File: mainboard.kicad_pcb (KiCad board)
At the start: 2 copper layers, 180 x 87 mm, 16 parts, among them J1 Raspi Pi Zero 2W, J2 LCD, J3 Keyboard, J4 USB_C_Receptacle_USB2.0, J5 Conn_02x20_Odd_Even, J6 Conn_02x20_Odd_Even, U1 MCP23017_SO

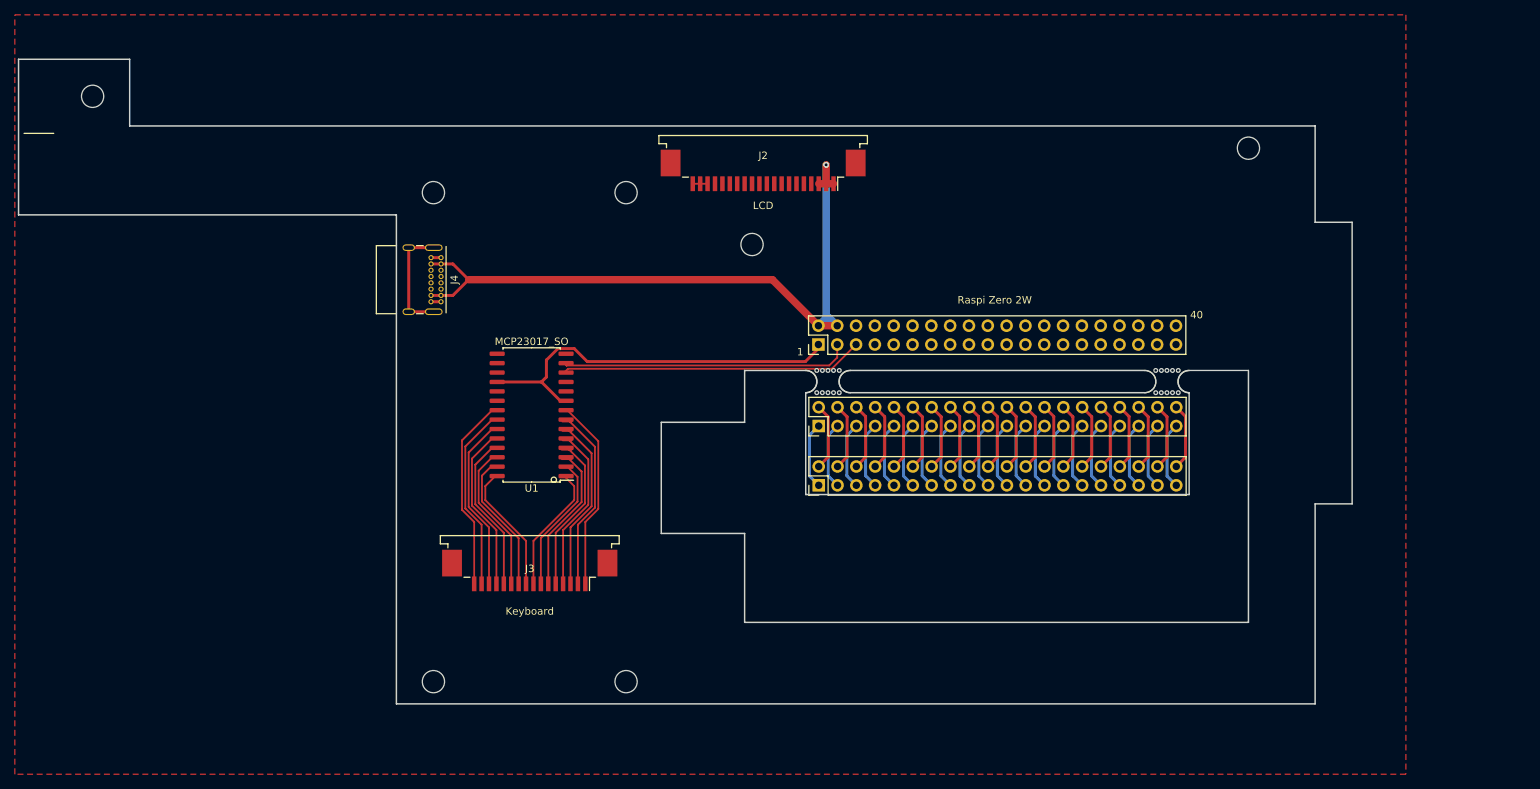
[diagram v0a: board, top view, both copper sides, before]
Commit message: adding logic converter and power supply
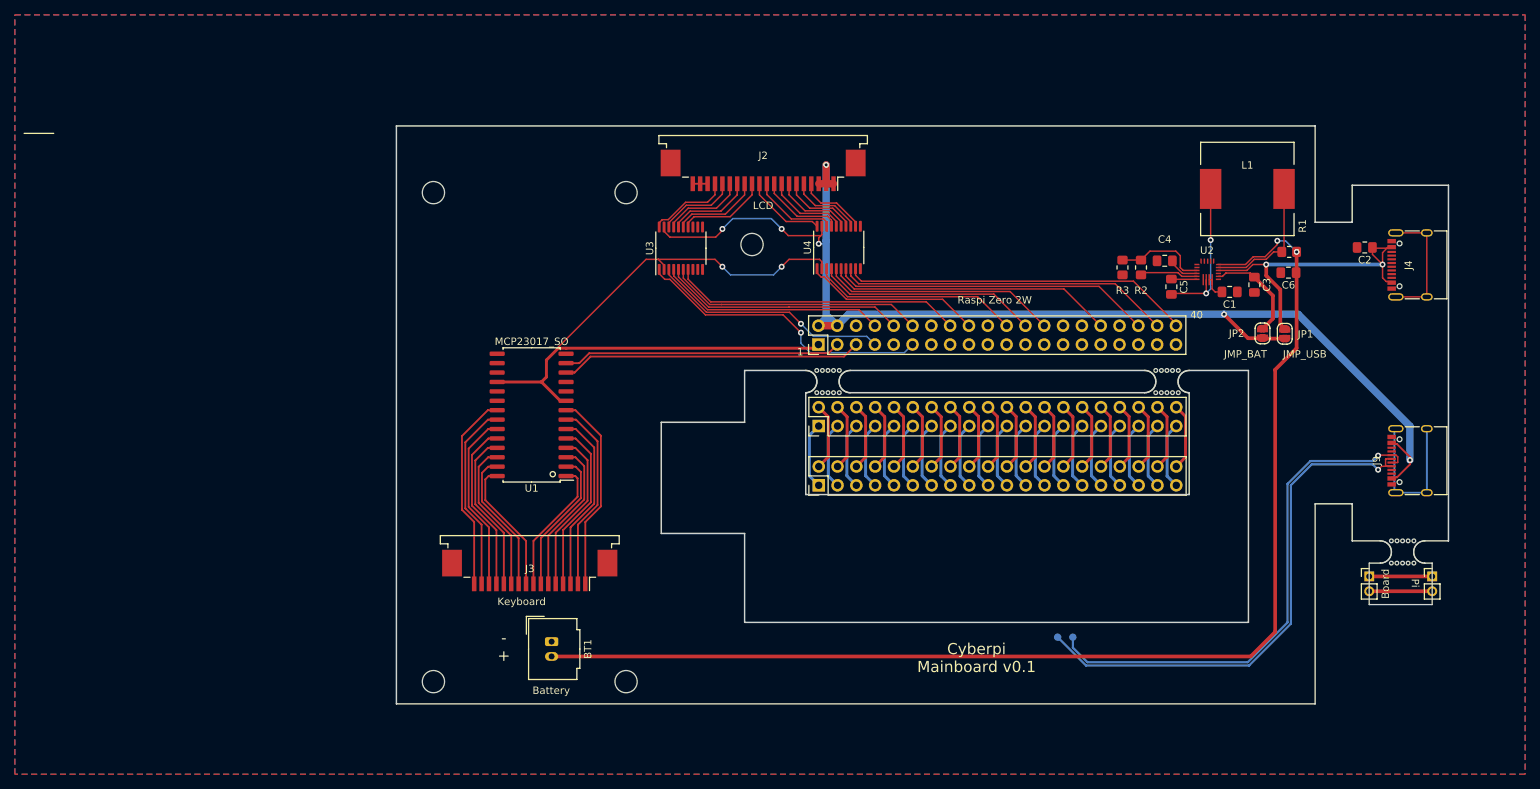
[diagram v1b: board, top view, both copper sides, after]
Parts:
- removed the REF** at (192.9, 59.4)
- removed the REF** at (36.9, 52.4)
- added BT1: Battery, Connector_Molex:Molex_MicroClasp_55932-0230_1x02_P2.00mm_Vertical, F.Cu at (98.8, 126.0)
- added C1: 10u 16V, Capacitor_SMD:C_0805_2012Metric_Pad1.18x1.45mm_HandSolder, F.Cu at (190.3, 78.8)
- added C2: 1u 16V, Capacitor_SMD:C_0805_2012Metric_Pad1.18x1.45mm_HandSolder, F.Cu at (208.6, 72.8)
- added C3: 10u 16V, Capacitor_SMD:C_0805_2012Metric_Pad1.18x1.45mm_HandSolder, F.Cu at (193.7, 77.8)
- added C4: 2.2u 6.3V, Capacitor_SMD:C_0805_2012Metric_Pad1.18x1.45mm_HandSolder, F.Cu at (181.6, 74.6)
- added C5: 470n 10V, Capacitor_SMD:C_0805_2012Metric_Pad1.18x1.45mm_HandSolder, F.Cu at (182.5, 78.1)
- added C6: 22u 10V, Capacitor_SMD:C_0805_2012Metric_Pad1.18x1.45mm_HandSolder, F.Cu at (198.3, 76.2)
- added J10: USBDataBoard, Connector_PinHeader_2.00mm:PinHeader_1x02_P2.00mm_Vertical, F.Cu at (209.2, 117.2)
- added J11: DM, TestPoint:TestPoint_Pad_D1.0mm, B.Cu at (167.1, 125.4)
- added J7: DP, TestPoint:TestPoint_Pad_D1.0mm, B.Cu at (169.2, 125.4)
- added J8: USBDataPi, Connector_PinHeader_2.00mm:PinHeader_1x02_P2.00mm_Vertical, F.Cu at (217.7, 117.2)
- added J9: USB Data, Connector_USB:USB_C_Receptacle_XKB_U262-16XN-4BVC11, F.Cu at (215.9, 101.6)
- added JP1: JMP_USB, Jumper:SolderJumper-2_P1.3mm_Open_RoundedPad1.0x1.5mm, F.Cu at (197.8, 84.5)
- added JP2: JMP_BAT, Jumper:SolderJumper-2_P1.3mm_Open_RoundedPad1.0x1.5mm, F.Cu at (194.8, 84.4)
- added L1: 1uH, Inductor_SMD:L_12x12mm_H4.5mm, F.Cu at (192.7, 64.9)
- added R1: 10m, Resistor_SMD:R_0805_2012Metric_Pad1.20x1.40mm_HandSolder, F.Cu at (198.4, 73.4)
- added R2: 10k, Resistor_SMD:R_0805_2012Metric_Pad1.20x1.40mm_HandSolder, F.Cu at (178.4, 75.5)
- added R3: 10k, Resistor_SMD:R_0805_2012Metric_Pad1.20x1.40mm_HandSolder, F.Cu at (175.9, 75.5)
- added U2: MP2696A, Library:QFN-21, F.Cu at (187.4, 76.1)
- added U3: TXS0108EPW, Package_SO:TSSOP-20_4.4x6.5mm_P0.65mm, F.Cu at (116.3, 72.9)
- added U4: TXS0108EPW, Package_SO:TSSOP-20_4.4x6.5mm_P0.65mm, F.Cu at (137.6, 72.8)
- added mouse-bite-3mm-slot: VAL**, Library:mouse-bite-3mm-slot, F.Cu at (213.7, 113.9)
- J4: value USB_C_Receptacle_USB2.0 -> USB Power; footprint Connector_USB:USB_C_Receptacle_GCT_USB4085 -> Connector_USB:USB_C_Receptacle_XKB_U262-16XN-4BVC11
- moved J4 132.0 mm to (215.9, 75.2), turned to 90 degrees
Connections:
- J1 pad 13: /GPIO_27 -> unconnected-(J1-Pad13)
- J1 pad 14: GND -> unconnected-(J1-Pad14)
- J1 pad 15: /GPIO_22 -> unconnected-(J1-Pad15)
- J1 pad 17: +3V3 -> unconnected-(J1-Pad17)
- J1 pad 19: /GPIO_10 -> unconnected-(J1-Pad19)
- J1 pad 20: GND -> unconnected-(J1-Pad20)
- J1 pad 21: /GPIO_9 -> unconnected-(J1-Pad21)
- J1 pad 23: /GPIO_11 -> unconnected-(J1-Pad23)
- J1 pad 27: /EEPROM_DATA -> unconnected-(J1-Pad27)
- J1 pad 28: /SCL0 -> unconnected-(J1-Pad28)
- J1 pad 29: /GPIO_5 -> unconnected-(J1-Pad29)
- J1 pad 30: GND -> unconnected-(J1-Pad30)
- J1 pad 31: /GPIO_6 -> unconnected-(J1-Pad31)
- J1 pad 33: /GPIO_13 -> unconnected-(J1-Pad33)
- J1 pad 34: GND -> unconnected-(J1-Pad34)
- J1 pad 35: /GPIO_19 -> unconnected-(J1-Pad35)
- J1 pad 37: /GPIO_26 -> unconnected-(J1-Pad37)
- J1 pad 6: GND -> unconnected-(J1-Pad6)
- J1 pad 9: GND -> unconnected-(J1-Pad9)
- J4 pad A4: +5V -> /Power Circuit/USBPWR
- J4 pad A9: +5V -> /Power Circuit/USBPWR
- J4 pad B4: +5V -> /Power Circuit/USBPWR
- J4 pad B9: +5V -> /Power Circuit/USBPWR
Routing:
- net Net-(BT1-Pad2): track 0.00 -> 164.4 mm, vias 0 -> 2
- net +5V: track 92.8 -> 164.8 mm, vias 1 -> 6
- net /D-: track 0.00 -> 71.9 mm, vias 0 -> 1
- net /D+: track 0.00 -> 70.3 mm, vias 0 -> 1
- net /GPIO_21: track 0.00 -> 47.1 mm
- net /GPIO_20: track 0.00 -> 45.1 mm
- net /Power Circuit/USBPWR: track 0.00 -> 44.2 mm, vias 0 -> 2
- net +3V3: track 52.9 -> 96.3 mm, vias 0 -> 2
- net /GPIO_16: track 0.00 -> 43.2 mm
- net /GPIO_17: track 0.00 -> 40.5 mm, vias 0 -> 1
- net /GPIO_23: track 0.00 -> 39.3 mm
- net /GPIO_12: track 0.00 -> 38.8 mm
- net /GPIO_18: track 0.00 -> 34.8 mm
- net /GPIO_15: track 0.00 -> 32.8 mm
- net /GPIO_4: track 0.00 -> 32.4 mm, vias 0 -> 1
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- added copper zone on B.Cu, net GND
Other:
- board size 180 x 87 mm -> 142 x 78 mm
- rule pad_to_mask_clearance: 0.051 -> 0
- board text added: "- +"
- board text added: "3mm"
- board text added: "Board"
- board text added: "Cyberpi Mainboard v0.1"
- board text added: "Data"
- board text added: "Pi"
- board text added: "Power"

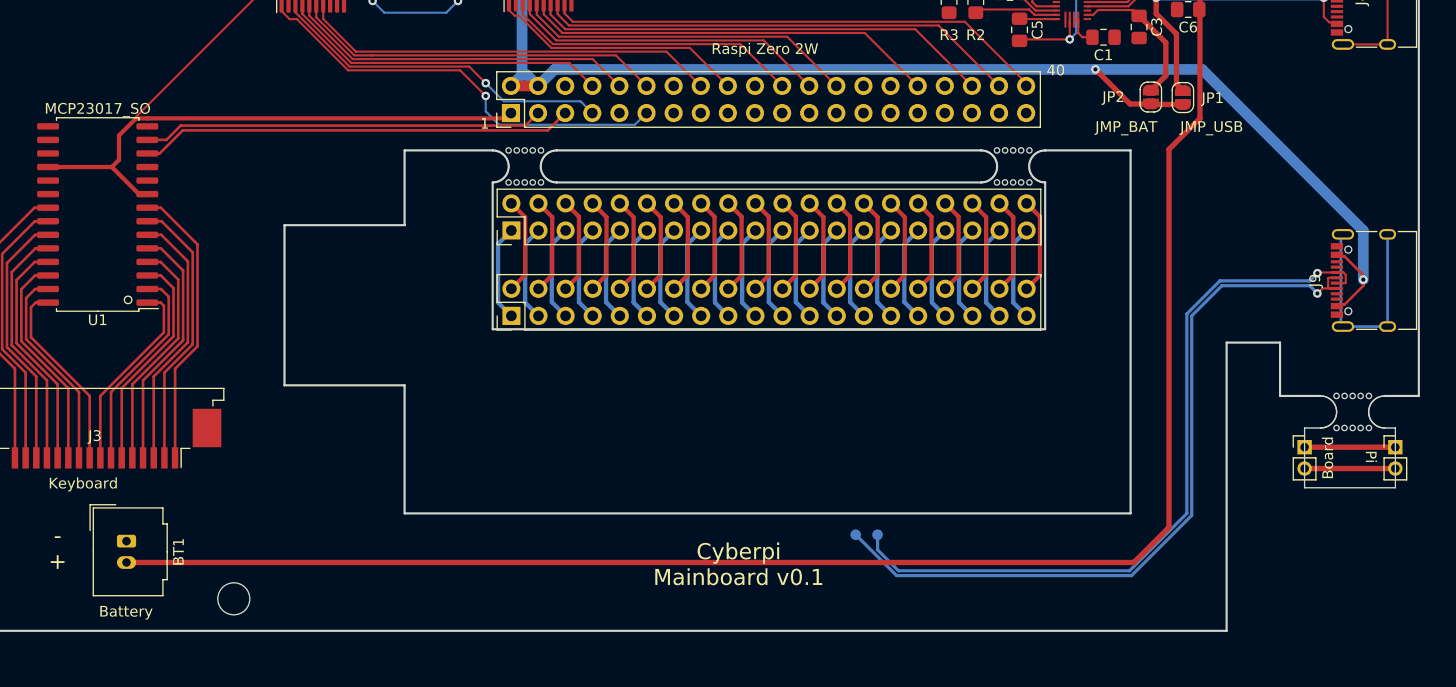
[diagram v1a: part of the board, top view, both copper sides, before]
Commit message: Adding switch to power
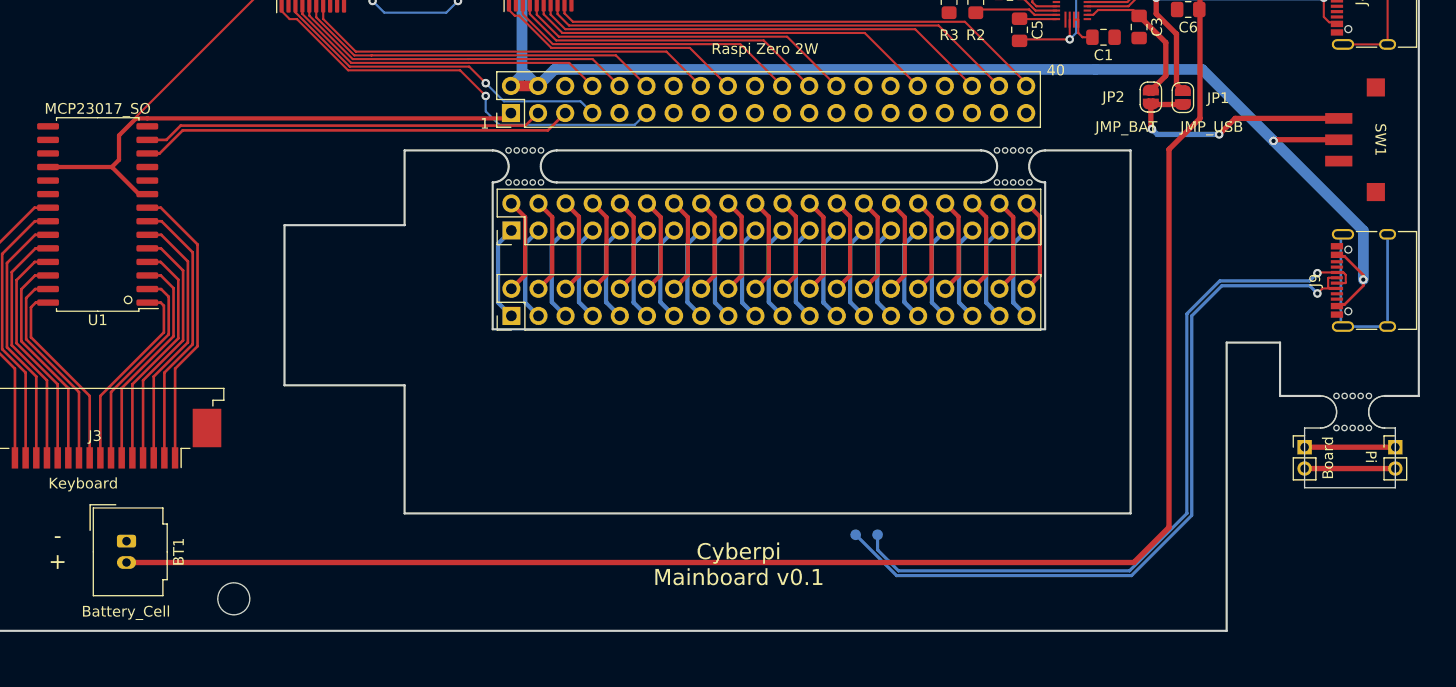
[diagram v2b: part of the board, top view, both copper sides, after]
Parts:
- added SW1: SW_SPST, Library:SS312SAH4-R, F.Cu at (215.5, 88.4)
- BT1: value Battery -> Battery_Cell
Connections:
- JP1 pad 2: +5V -> Net-(JP1-Pad2)
- JP2 pad 2: +5V -> Net-(JP1-Pad2)
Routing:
- net Net-(JP1-Pad2): track 0.00 -> 23.7 mm, vias 0 -> 2
- net +5V: track 164.8 -> 161.4 mm
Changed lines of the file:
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@@
   (net 151 "unconnected-(J1-Pad35)")
   (net 152 "unconnected-(J1-Pad37)")
+  (net 153 "Net-(JP1-Pad2)")
   (footprint "MountingHole:MountingHole_3mm" locked (layer "F.Cu")
     (at 108.86 131.4)
@@
       (effects (font (size 1 1) (thickness 0.15)))
     )
-    (fp_text value "Battery" (at 6.6 0.05 180) (layer "F.SilkS")
+    (fp_text value "Battery_Cell" (at 6.6 0.05 180) (layer "F.SilkS")
       (effects (font (size 1 1) (thickness 0.15)))
     )
@@
       ))
     (pad "2" smd custom (at 0.65 0 270) (size 1 0.5) (layers "F.Cu" "F.Mask")
-      (net 1 "+5V") (pinfunction "B") (pintype "passive") (zone_connect 2)
+      (net 153 "Net-(JP1-Pad2)") (pinfunction "B") (pintype "passive") (zone_connect 2)
       (options (clearance outline) (anchor rect))
       (primitives
@@
     (property "Sheetname" "")
     (attr exclude_from_pos_files)
-    (fp_text reference "JP1" (at 0.05 -2.8 180) (layer "F.SilkS")
+    (fp_text reference "JP1" (at 0.05 -3.3 180) (layer "F.SilkS")
       (effects (font (size 1 1) (thickness 0.15)))
     )
@@
       ))
     (pad "2" smd custom (at 0.65 0 270) (size 1 0.5) (layers "F.Cu" "F.Mask")
-      (net 1 "+5V") (pinfunction "B") (pintype "passive") (zone_connect 2)
+      (net 153 "Net-(JP1-Pad2)") (pinfunction "B") (pintype "passive") (zone_connect 2)
       (options (clearance outline) (anchor rect))
       (primitives
@@
     )
   )
+  (footprint "Library:SS312SAH4-R" (layer "F.Cu")
+    (at 215.46 88.4 180)
+    (property "Sheetfile" "mainboard.kicad_sch")
+    (property "Sheetname" "")
+    (attr smd)
+    (fp_text reference "SW1" (at -0.8 0 270 unlocked) (layer "F.SilkS")
+      (effects (font (size 1 1) (thickness 0.15)))
+    )
+    (fp_text value "SW_SPST" (at 0.9 -0.1 270 unlocked) (layer "F.Fab")
+      (effects (font (size 1 1) (thickness 0.15)))
+    )
+    (fp_text user "${REFERENCE}" (at -0.8 0 270 unlocked) (layer "F.Fab")
+      (effects (font (size 1 1) (thickness 0.15)))
+    )
+    (fp_rect (start -1.8 2) (end -3.8 -2) (layer "F.Fab") (width 0.05) (fill none))
+    (fp_rect (start -1.8 -4.6) (end 2.2 4.6) (layer "F.Fab") (width 0.05) (fill none))
+    (pad "1" smd rect (at 3.1 2 180) (size 2.55 1) (layers "F.Cu" "F.Paste" "F.Mask")
+      (net 153 "Net-(JP1-Pad2)") (pinfunction "A") (pintype "passive"))
+    (pad "2" smd rect (at 3.1 0 180) (size 2.55 1) (layers "F.Cu" "F.Paste" "F.Mask")
+      (net 1 "+5V") (pinfunction "B") (pintype "passive"))
+    (pad "3" smd rect (at 3.1 -2 180) (size 2.55 1) (layers "F.Cu" "F.Paste" "F.Mask"))
+    (pad "NC" smd rect (at -0.375 4.9 180) (size 1.7 1.7) (layers "F.Cu" "F.Paste" "F.Mask"))
+    (pad "NC" smd rect (at -0.375 -4.9 180) (size 1.7 1.7) (layers "F.Cu" "F.Paste" "F.Mask"))
+  )
   (footprint "Capacitor_SMD:C_0805_2012Metric_Pad1.18x1.45mm_HandSolder" (layer "F.Cu")
     (at 198.26 76.2 180)
@@
   (segment (start 212.19 99.33) (end 212.905727 99.33) (width 0.25) (layer "F.Cu") (net 1))
   (segment (start 214.66 102.075727) (end 214.66 101.5) (width 0.25) (layer "F.Cu") (net 1))
-  (segment (start 192.81 85.05) (end 189.570489 81.810489) (width 0.5) (layer "F.Cu") (net 1))
   (segment (start 120.957038 71.4) (end 114.765705 71.4) (width 0.2) (layer "F.Cu") (net 1))
-  (segment (start 197.76 85.1) (end 194.81 85.1) (width 0.5) (layer "F.Cu") (net 1))
   (segment (start 114.765705 71.4) (end 113.985 70.619295) (width 0.2) (layer "F.Cu") (net 1))
-  (segment (start 194.81 85.1) (end 194.76 85.05) (width 0.5) (layer "F.Cu") (net 1))
   (segment (start 113.985 70.619295) (end 113.985 70.0375) (width 0.2) (layer "F.Cu") (net 1))
   (segment (start 214.66 101.084273) (end 214.66 101.5) (width 0.25) (layer "F.Cu") (net 1))
@@
   (segment (start 135.86 64.2) (end 134.864511 64.2) (width 1) (layer "F.Cu") (net 1))
   (segment (start 135.285 71.075) (end 135.16 71.2) (width 0.2) (layer "F.Cu") (net 1))
+  (segment (start 206.36 88.4) (end 206.250688 88.509312) (width 0.5) (layer "F.Cu") (net 1))
   (segment (start 137.36 83.36) (end 134.82 83.36) (width 1) (layer "F.Cu") (net 1))
   (segment (start 212.905727 99.33) (end 214.66 101.084273) (width 0.25) (layer "F.Cu") (net 1))
   (segment (start 129.86 70.3) (end 130.76 71.2) (width 0.2) (layer "F.Cu") (net 1))
-  (segment (start 194.76 85.05) (end 192.81 85.05) (width 0.5) (layer "F.Cu") (net 1))
   (segment (start 212.19 103.83) (end 212.905727 103.83) (width 0.25) (layer "F.Cu") (net 1))
   (segment (start 134.86 71.5) (end 134.86 72.3) (width 0.2) (layer "F.Cu") (net 1))
   (segment (start 135.285 69.9375) (end 135.285 71.075) (width 0.2) (layer "F.Cu") (net 1))
+  (segment (start 212.36 88.4) (end 206.36 88.4) (width 0.5) (layer "F.Cu") (net 1))
   (segment (start 135.86 64.2) (end 135.86 61.65) (width 1) (layer "F.Cu") (net 1))
   (segment (start 212.905727 103.83) (end 214.66 102.075727) (width 0.25) (layer "F.Cu") (net 1))
@@
   (segment (start 121.86 70.497038) (end 120.957038 71.4) (width 0.2) (layer "F.Cu") (net 1))
   (segment (start 135.86 64.2) (end 136.86 64.2) (width 1) (layer "F.Cu") (net 1))
-  (via (at 189.570489 81.810489) (size 0.8) (drill 0.4) (layers "F.Cu" "B.Cu") (net 1))
   (via (at 135.86 61.65) (size 0.8) (drill 0.4) (layers "F.Cu" "B.Cu") (net 1))
   (via (at 134.86 72.3) (size 0.8) (drill 0.4) (layers "F.Cu" "B.Cu") (net 1))
   (via (at 214.66 101.5) (size 0.8) (drill 0.4) (layers "F.Cu" "B.Cu") (net 1))
   (via (at 129.86 70.3) (size 0.8) (drill 0.4) (layers "F.Cu" "B.Cu") (net 1))
+  (via (at 206.250688 88.509312) (size 0.8) (drill 0.4) (layers "F.Cu" "B.Cu") (net 1))
   (via (at 121.86 70.3) (size 0.8) (drill 0.4) (layers "F.Cu" "B.Cu") (net 1))
   (segment (start 135.86 82.32) (end 134.82 83.36) (width 1) (layer "B.Cu") (net 1))
@@
   (segment (start 134.86 72.3) (end 135.46 72.3) (width 0.2) (layer "B.Cu") (net 1))
   (segment (start 121.86 70.3) (end 123.26 68.9) (width 0.2) (layer "B.Cu") (net 1))
+  (segment (start 206.250688 88.509312) (end 214.66 96.918623) (width 1) (layer "B.Cu") (net 1))
   (segment (start 128.46 68.9) (end 129.86 70.3) (width 0.2) (layer "B.Cu") (net 1))
   (segment (start 123.26 68.9) (end 128.46 68.9) (width 0.2) (layer "B.Cu") (net 1))
@@
   (segment (start 138.909511 81.810489) (end 189.570489 81.810489) (width 1) (layer "B.Cu") (net 1))
   (segment (start 137.36 83.36) (end 138.909511 81.810489) (width 1) (layer "B.Cu") (net 1))
+  (segment (start 199.551866 81.810489) (end 206.250688 88.509312) (width 1) (layer "B.Cu") (net 1))
   (segment (start 189.570489 81.810489) (end 199.551866 81.810489) (width 1) (layer "B.Cu") (net 1))
-  (segment (start 199.551866 81.810489) (end 214.66 96.918623) (width 1) (layer "B.Cu") (net 1))
   (segment (start 135.86 61.65) (end 135.86 71.9) (width 1) (layer "B.Cu") (net 1))
   (segment (start 136.585 76.625) (end 136.585 75.6625) (width 0.2) (layer "F.Cu") (net 2))
@@
   (segment (start 193.66 76.8) (end 196.16 79.3) (width 0.5) (layer "F.Cu") (net 129))
   (segment (start 189.359022 76.7) (end 189.809502 76.24952) (width 0.2) (layer "F.Cu") (net 129))
+  (segment (start 197.76 85.1) (end 194.81 85.1) (width 0.5) (layer "F.Cu") (net 153))
+  (segment (start 201.16 87.9) (end 202.66 86.4) (width 0.5) (layer "F.Cu") (net 153))
+  (segment (start 202.66 86.4) (end 212.36 86.4) (width 0.5) (layer "F.Cu") (net 153))
+  (segment (start 194.81 85.1) (end 194.76 85.05) (width 0.5) (layer "F.Cu") (net 153))
+  (segment (start 194.86 87.4) (end 194.76 87.3) (width 0.5) (layer "F.Cu") (net 153))
+  (segment (start 194.76 87.3) (end 194.76 85.05) (width 0.5) (layer "F.Cu") (net 153))
+  (via (at 194.86 87.4) (size 0.8) (drill 0.4) (layers "F.Cu" "B.Cu") (net 153))
+  (via (at 201.16 87.9) (size 0.8) (drill 0.4) (layers "F.Cu" "B.Cu") (net 153))
+  (segment (start 195.36 87.9) (end 201.16 87.9) (width 0.5) (layer "B.Cu") (net 153))
+  (segment (start 194.86 87.4) (end 195.36 87.9) (width 0.5) (layer "B.Cu") (net 153))
   (zone (net 4) (net_name "GND") (layers F&B.Cu) (hatch edge 0.508)
     (connect_pads (clearance 0.2))
